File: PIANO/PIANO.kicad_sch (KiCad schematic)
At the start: 33 parts, among them J1 Conn_01x02_Male, J2 USB_B_Micro, SW1 ON/OFF, SW2 RESET, U1 LF33_TO220, U2 ESP32-S2-SOLO, U3 Opamp_Dual, U4 Opamp_Dual

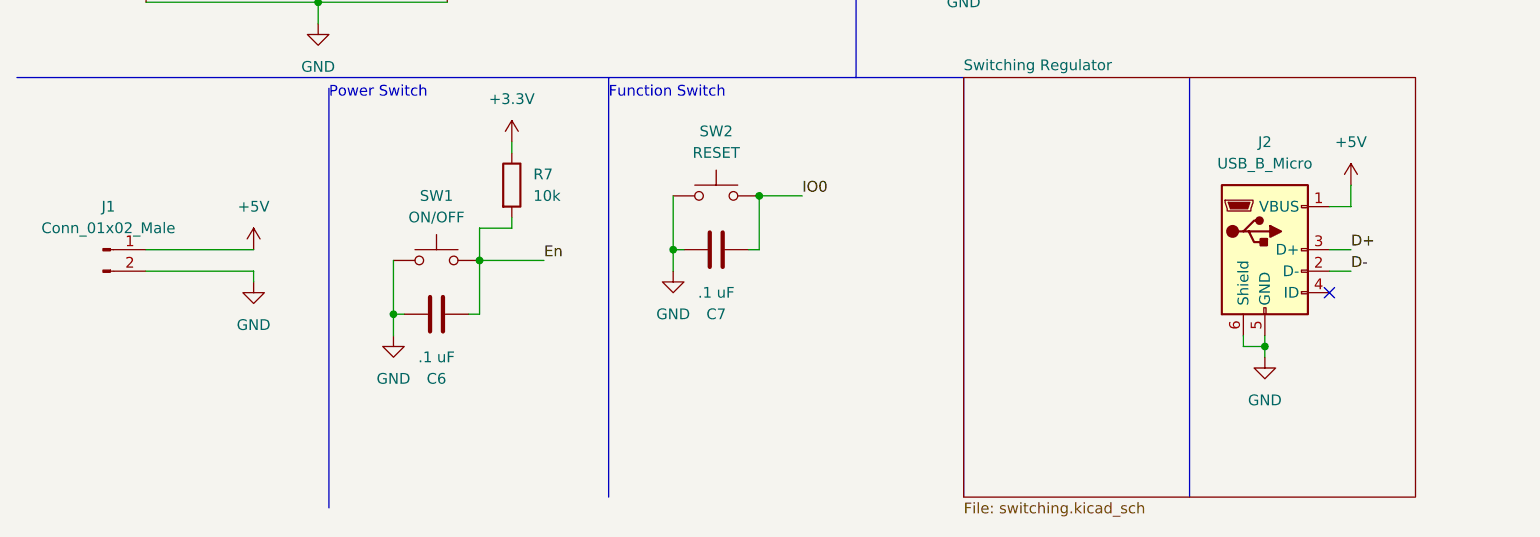
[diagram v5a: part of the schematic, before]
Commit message: Bathroom Trip Commit
Did the circuit for most of the regulator
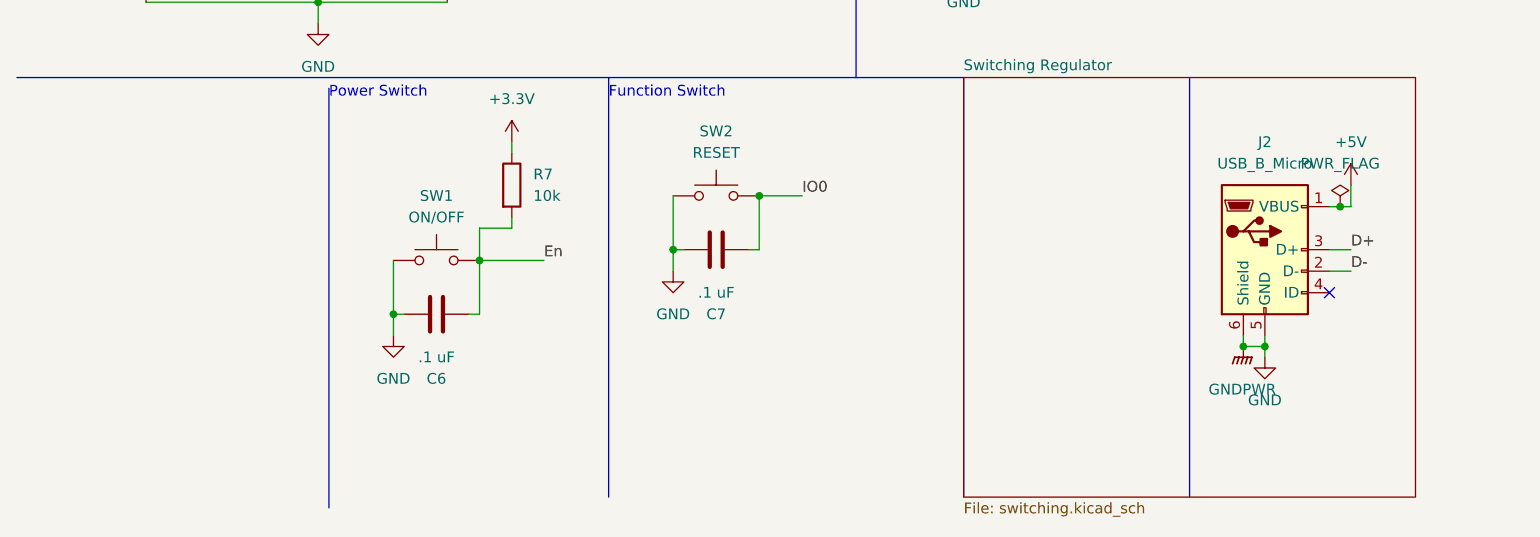
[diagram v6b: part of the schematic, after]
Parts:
- removed J1: Conn_01x02_Male, Connector_PinHeader_2.54mm:PinHeader_1x02_P2.54mm_Vertical, symbol Connector:Conn_01x02_Male
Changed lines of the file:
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@@
   (junction (at 212.09 105.41) (diameter 0) (color 0 0 0 0)
   )
+  (junction (at 156.21 180.34) (diameter 0) (color 0 0 0 0)
+  )
   (junction (at 210.82 43.18) (diameter 0) (color 0 0 0 0)
   )
@@
   )
   (junction (at 176.53 102.87) (diameter 0) (color 0 0 0 0)
+  )
+  (junction (at 167.64 163.83) (diameter 0) (color 0 0 0 0)
   )
   (junction (at 201.93 120.65) (diameter 0) (color 0 0 0 0)
@@
     (stroke (width 0) (type default) (color 0 0 0 0))
   )
+  (wire (pts (xy 167.64 163.83) (xy 168.91 163.83))
+    (stroke (width 0) (type default) (color 0 0 0 0))
+  )
   (wire (pts (xy 53.34 137.16) (xy 46.99 137.16))
     (stroke (width 0) (type default) (color 0 0 0 0))
@@
     (stroke (width 0) (type default) (color 0 0 0 0))
   )
-  (wire (pts (xy 26.67 171.45) (xy 39.37 171.45))
-    (stroke (width 0) (type default) (color 0 0 0 0))
-  )
   (polyline (pts (xy 12.7 105.41) (xy 110.49 105.41))
     (stroke (width 0) (type default) (color 0 0 0 0))
@@
     (stroke (width 0) (type default) (color 0 0 0 0))
   )
-  (wire (pts (xy 39.37 171.45) (xy 39.37 172.72))
-    (stroke (width 0) (type default) (color 0 0 0 0))
-  )
   (wire (pts (xy 52.07 35.56) (xy 72.39 35.56))
     (stroke (width 0) (type default) (color 0 0 0 0))
@@
     (stroke (width 0) (type default) (color 0 0 0 0))
   )
-  (wire (pts (xy 26.67 168.91) (xy 39.37 168.91))
-    (stroke (width 0) (type default) (color 0 0 0 0))
-  )
   (wire (pts (xy 219.71 30.48) (xy 219.71 34.29))
     (stroke (width 0) (type default) (color 0 0 0 0))
@@
     (stroke (width 0) (type default) (color 0 0 0 0))
   )
-  (wire (pts (xy 166.37 163.83) (xy 168.91 163.83))
+  (wire (pts (xy 166.37 163.83) (xy 167.64 163.83))
     (stroke (width 0) (type default) (color 0 0 0 0))
   )
@@
     (pin "1")
     (pin "2")
+  )
+  (symbol (lib_id "power:PWR_FLAG") (at 167.64 163.83 0) (unit 1)
+    (in_bom yes) (on_board yes) (fields_autoplaced)
+    (property "Reference" "#FLG0105" (id 0) (at 167.64 161.925 0)
+      (effects (font (size 1.27 1.27)) hide)
+    )
+    (property "Value" "PWR_FLAG" (id 1) (at 167.64 158.75 0))
+    (property "Footprint" "" (id 2) (at 167.64 163.83 0)
+      (effects (font (size 1.27 1.27)) hide)
+    )
+    (property "Datasheet" "~" (id 3) (at 167.64 163.83 0)
+      (effects (font (size 1.27 1.27)) hide)
+    )
+    (pin "1")
   )
   (symbol (lib_id "power:+3.3V") (at 62.23 120.65 0) (unit 1)
@@
     (pin "2")
   )
-  (symbol (lib_id "power:+5V") (at 39.37 168.91 0) (unit 1)
-    (in_bom yes) (on_board yes) (fields_autoplaced)
-    (property "Reference" "#PWR0126" (id 0) (at 39.37 172.72 0)
-      (effects (font (size 1.27 1.27)) hide)
-    )
-    (property "Value" "+5V" (id 1) (at 39.37 163.83 0))
-    (property "Footprint" "" (id 2) (at 39.37 168.91 0)
-      (effects (font (size 1.27 1.27)) hide)
-    )
-    (property "Datasheet" "" (id 3) (at 39.37 168.91 0)
-      (effects (font (size 1.27 1.27)) hide)
-    )
-    (pin "1")
-  )
   (symbol (lib_id "power:PWR_FLAG") (at 39.37 121.92 0) (unit 1)
     (in_bom yes) (on_board yes) (fields_autoplaced)
@@
     (pin "7")
   )
-  (symbol (lib_id "power:GND") (at 39.37 172.72 0) (unit 1)
-    (in_bom yes) (on_board yes) (fields_autoplaced)
-    (property "Reference" "#PWR0127" (id 0) (at 39.37 179.07 0)
-      (effects (font (size 1.27 1.27)) hide)
-    )
-    (property "Value" "GND" (id 1) (at 39.37 177.8 0))
-    (property "Footprint" "" (id 2) (at 39.37 172.72 0)
-      (effects (font (size 1.27 1.27)) hide)
-    )
-    (property "Datasheet" "" (id 3) (at 39.37 172.72 0)
+  (symbol (lib_id "power:GNDPWR") (at 156.21 180.34 0) (unit 1)
+    (in_bom yes) (on_board yes) (fields_autoplaced)
+    (property "Reference" "#PWR0138" (id 0) (at 156.21 185.42 0)
+      (effects (font (size 1.27 1.27)) hide)
+    )
+    (property "Value" "GNDPWR" (id 1) (at 156.083 185.42 0))
+    (property "Footprint" "" (id 2) (at 156.21 181.61 0)
+      (effects (font (size 1.27 1.27)) hide)
+    )
+    (property "Datasheet" "" (id 3) (at 156.21 181.61 0)
       (effects (font (size 1.27 1.27)) hide)
     )
@@
     (pin "1")
   )
-  (symbol (lib_id "Connector:Conn_01x02_Male") (at 21.59 168.91 0) (unit 1)
-    (in_bom yes) (on_board yes) (fields_autoplaced)
-    (property "Reference" "J1" (id 0) (at 22.225 163.83 0))
-    (property "Value" "Conn_01x02_Male" (id 1) (at 22.225 166.37 0))
-    (property "Footprint" "Connector_PinHeader_2.54mm:PinHeader_1x02_P2.54mm_Vertical" (id 2) (at 21.59 168.91 0)
-      (effects (font (size 1.27 1.27)) hide)
-    )
-    (property "Datasheet" "~" (id 3) (at 21.59 168.91 0)
-      (effects (font (size 1.27 1.27)) hide)
-    )
-    (pin "1")
-    (pin "2")
-  )
   (symbol (lib_id "power:+3.3V") (at 29.21 93.98 0) (unit 1)
     (in_bom yes) (on_board yes) (fields_autoplaced)
@@
       (reference "#FLG0103") (unit 1) (value "PWR_FLAG") (footprint "")
     )
+    (path "/7f576ece-c9bc-4f26-b53f-08232bf521db/1406e16c-b05a-4789-95a1-f137eaf3c632"
+      (reference "#FLG0104") (unit 1) (value "PWR_FLAG") (footprint "")
+    )
+    (path "/4f55f6e8-f43a-49af-b006-7872de1c336f"
+      (reference "#FLG0105") (unit 1) (value "PWR_FLAG") (footprint "")
+    )
     (path "/259c005d-0776-4b83-b48d-1b3691cec4a1"
       (reference "#PWR0101") (unit 1) (value "GND") (footprint "")
@@
       (reference "#PWR0125") (unit 1) (value "GND") (footprint "")
     )
-    (path "/6d0fcfab-1489-4b20-9a6e-8f03fde820ca"
-      (reference "#PWR0126") (unit 1) (value "+5V") (footprint "")
-    )
-    (path "/7b0390e3-cb04-40a0-8a44-04ff72f542fb"
-      (reference "#PWR0127") (unit 1) (value "GND") (footprint "")
-    )
     (path "/7f576ece-c9bc-4f26-b53f-08232bf521db/93e95753-b550-4032-9af7-012ce2fbe4f7"
       (reference "#PWR0128") (unit 1) (value "GND") (footprint "")
@@
       (reference "#PWR0131") (unit 1) (value "+5V") (footprint "")
     )
+    (path "/7f576ece-c9bc-4f26-b53f-08232bf521db/6bfb23de-870c-417a-a5b3-52a99a51d307"
+      (reference "#PWR0132") (unit 1) (value "+5V") (footprint "")
+    )
     (path "/7f576ece-c9bc-4f26-b53f-08232bf521db/f0b7f140-6667-44f5-a73a-11f6423c8f34"
       (reference "#PWR0133") (unit 1) (value "GND") (footprint "")
@@
       (reference "#PWR0135") (unit 1) (value "GND") (footprint "")
     )
+    (path "/7f576ece-c9bc-4f26-b53f-08232bf521db/bc0e4c96-fb93-4f51-b821-28901512cfd9"
+      (reference "#PWR0136") (unit 1) (value "+9V") (footprint "")
+    )
+    (path "/7f576ece-c9bc-4f26-b53f-08232bf521db/f9db4a6b-0fb6-4624-9b2c-394a4032d24c"
+      (reference "#PWR0137") (unit 1) (value "+9V") (footprint "")
+    )
+    (path "/7c282dd2-e10f-44df-9bc9-b6869d284865"
+      (reference "#PWR0138") (unit 1) (value "GNDPWR") (footprint "")
+    )
     (path "/7f05d072-22d9-4098-ad43-15fc4a4844a4"
       (reference "C1") (unit 1) (value "10 uF") (footprint "Capacitor_SMD:C_0805_2012Metric")
@@
       (reference "D5") (unit 1) (value "D_Schottky") (footprint "Diode_SMD:D_SOD-123F")
     )
-    (path "/a8eec9a6-5455-454a-8104-384cf0571e04"
-      (reference "J1") (unit 1) (value "Conn_01x02_Male") (footprint "Connector_PinHeader_2.54mm:PinHeader_1x02_P2.54mm_Vertical")
-    )
     (path "/0ccf3bde-866e-4231-b785-fc8e0833134f"

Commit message: try again
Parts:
- removed LS1: Speaker, Sensor_Audio:CUI_CMC-4013-SMT, symbol Device:Speaker
- removed unit 2 of U3
- added J4: 22-23-2021, digikey-footprints:PinHeader_1x2_P2.54mm_Drill1.02mm, symbol dk_Rectangular-Connectors-Headers-Male-Pins:22-23-2021
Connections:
- net +5V: no longer J2.1 (VBUS)
- net GND: now also J4.1
- net Output: no longer U2.4 (GPIO4/TOUCH4/ADC1_CH3), U3.3 (+)
- net at R8.1, U3.1: now also J4.2
- net Spkr 2: now reaches U2.5 (GPIO5/TOUCH5/ADC1_CH4)
- new net Spkr 1: U2.4 (GPIO4/TOUCH4/ADC1_CH3), U3.3 (+)
- no-connect marks 33 -> 30
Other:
- added sheet Ext_Spkr2 (Ext_Spkr2_sch.kicad_sch)

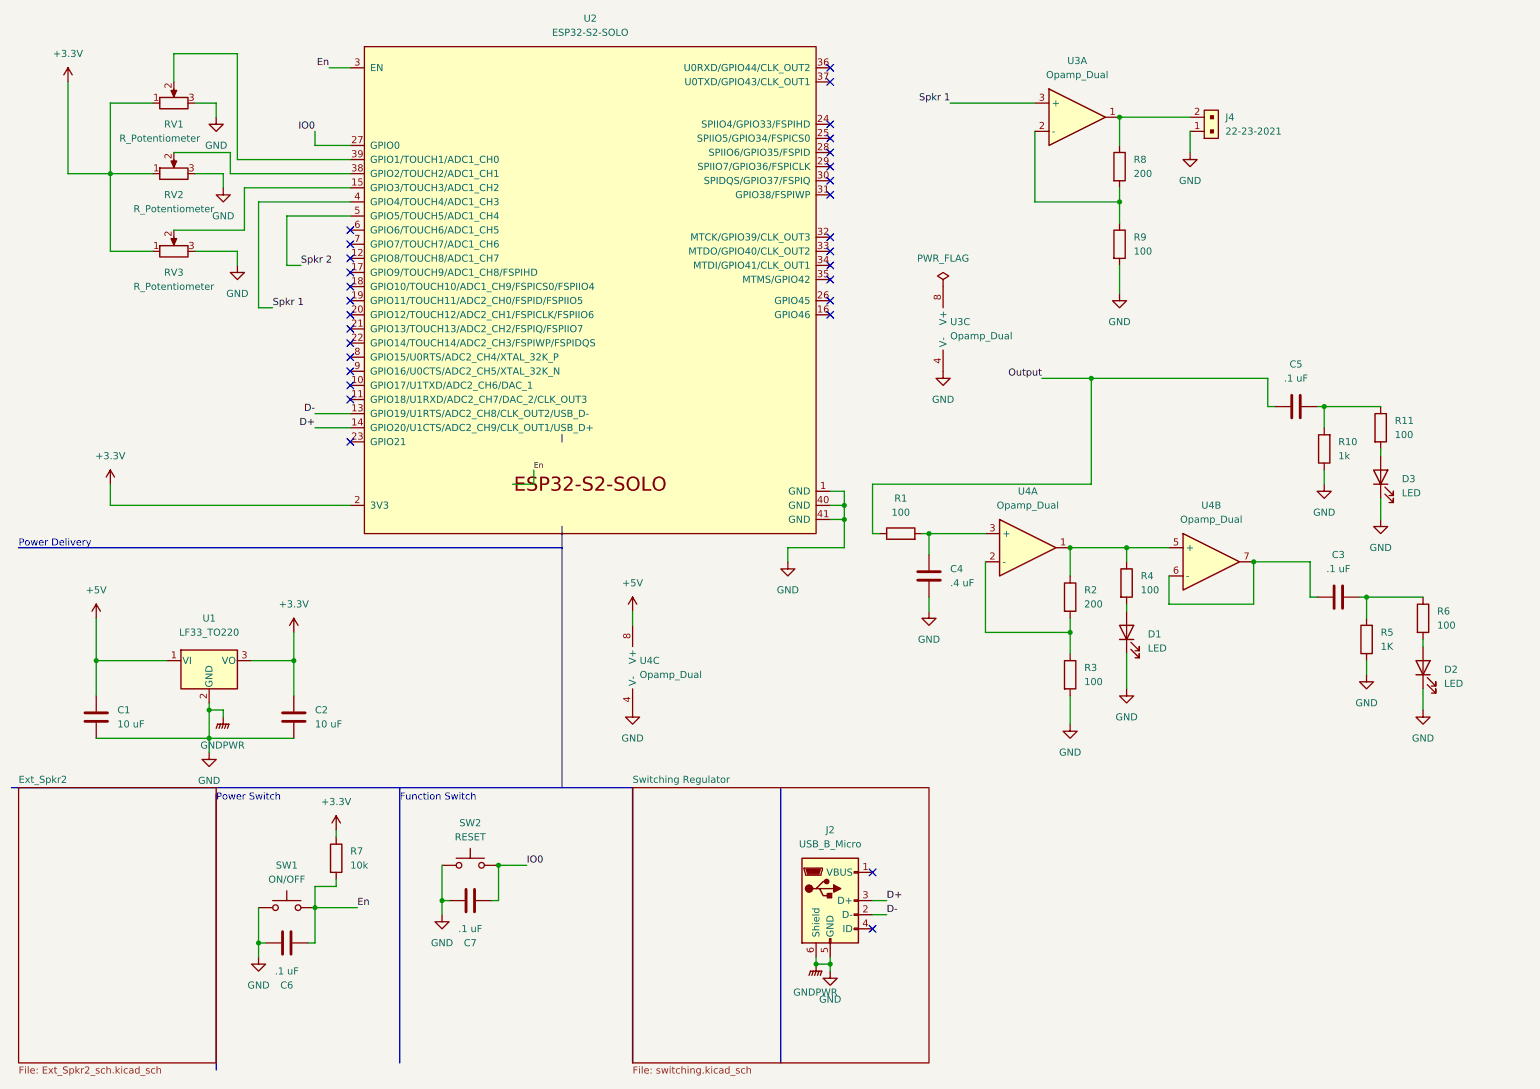
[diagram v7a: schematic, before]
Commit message: added pin headers waiting for check
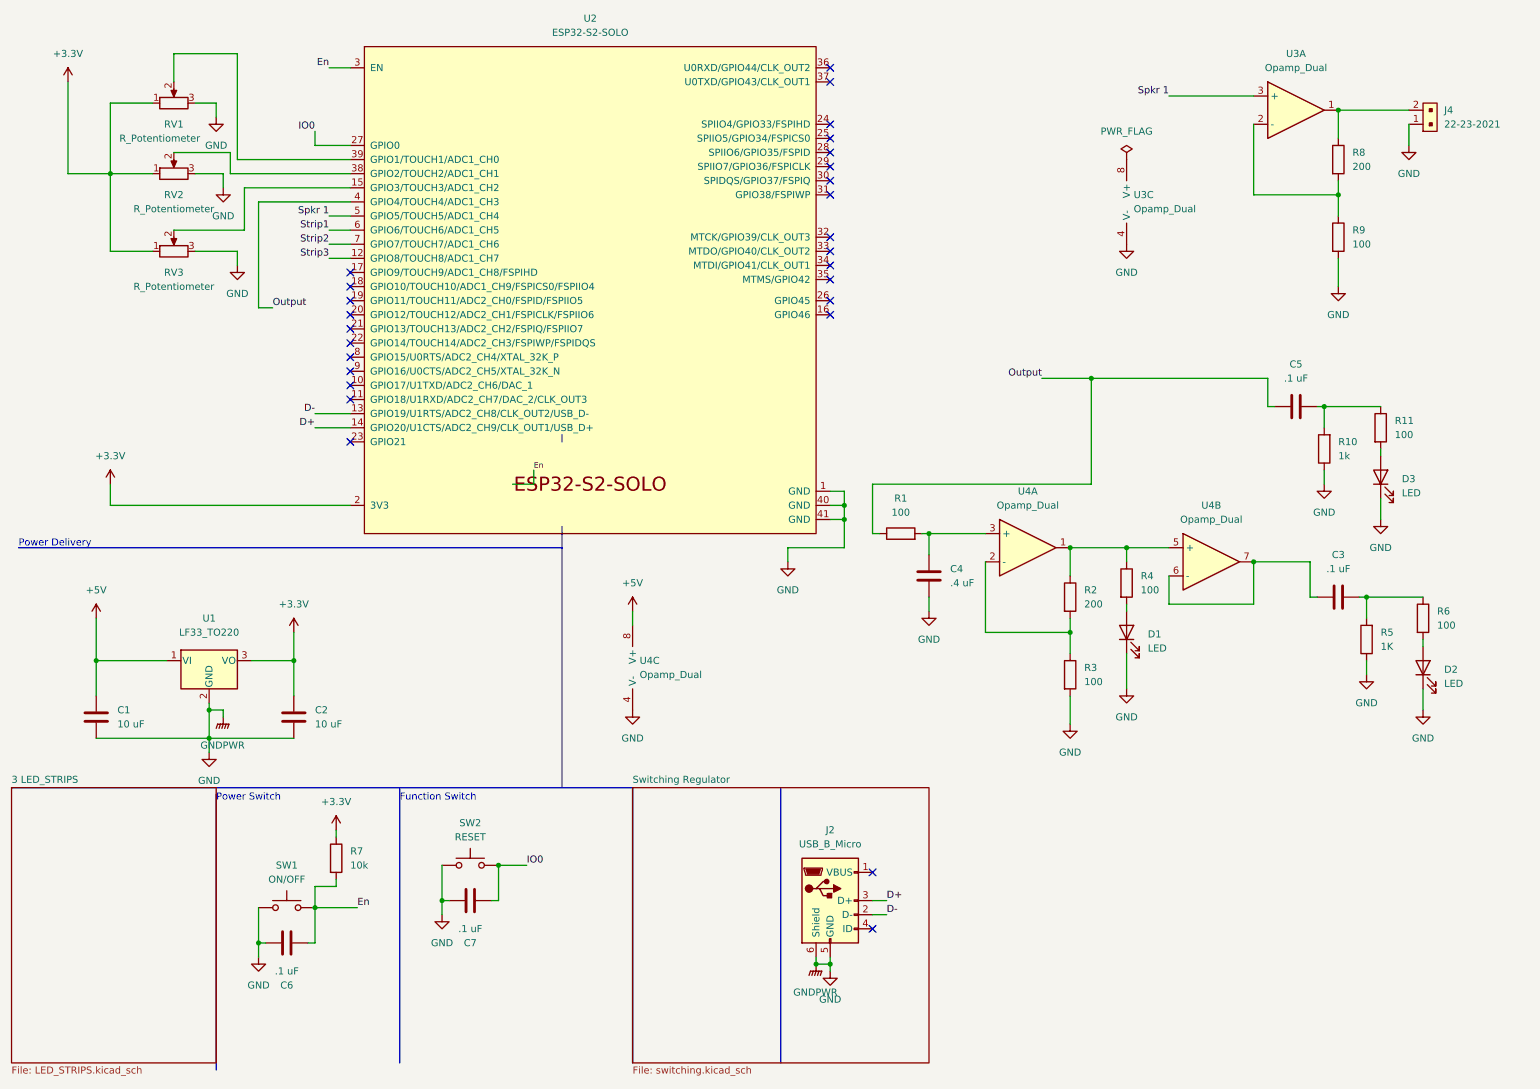
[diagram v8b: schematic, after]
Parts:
- J4: footprint digikey-footprints:PinHeader_1x2_P2.54mm_Drill1.02mm -> Connector_PinHeader_1.00mm:PinHeader_1x02_P1.00mm_Vertical
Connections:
- net Spkr 2 is gone; now on net Spkr 1: U2.5 (GPIO5/TOUCH5/ADC1_CH4)
- net Output: now also U2.4 (GPIO4/TOUCH4/ADC1_CH3)
- net Spkr 1: no longer U2.4 (GPIO4/TOUCH4/ADC1_CH3)
- net Strip3: now reaches U2.12 (GPIO8/TOUCH8/ADC1_CH7)
- net Strip1: now reaches U2.6 (GPIO6/TOUCH6/ADC1_CH5)
- net Strip2: now reaches U2.7 (GPIO7/TOUCH7/ADC1_CH6)
- no-connect marks 30 -> 27
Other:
- removed sheet Ext_Spkr2
- added sheet 3 LED_STRIPS (LED_STRIPS.kicad_sch)
- moved on the sheet: J4, R8, R9, U3A, U3C
